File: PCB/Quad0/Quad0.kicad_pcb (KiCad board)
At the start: 4 copper layers, 50.1 x 50.1 mm, 97 parts, among them J1 DEBUG_CONN_PAD, J10 GPIO[23-24], J2 Mtype_Select, J3 Mtype_Select, J4 Mtype_Select, J5 Mtype_Select, J6 1N5819, J7 Power_Pad, J8 GPIO[18-22], J9 GPIO[27-29], Q1 DMN2024UFDF-7, Q2 DMN2024UFDF-7, Q3 DMN2024UFDF-7, Q4 DMN2024UFDF-7, SW1 RUN_BTN, SW2 BOOTSEL_BTN, U1 RP2350A_C42411118, U2 AP7361C-33E-13, U3 W25Q128JVSIQTR, U4 ABM8-272-T3_C20625731, U5 ICM-42688-P, U6 DPS368XTSA1, U7 BMM150, U8 ESP-01, U9 AP22818BKWT-7

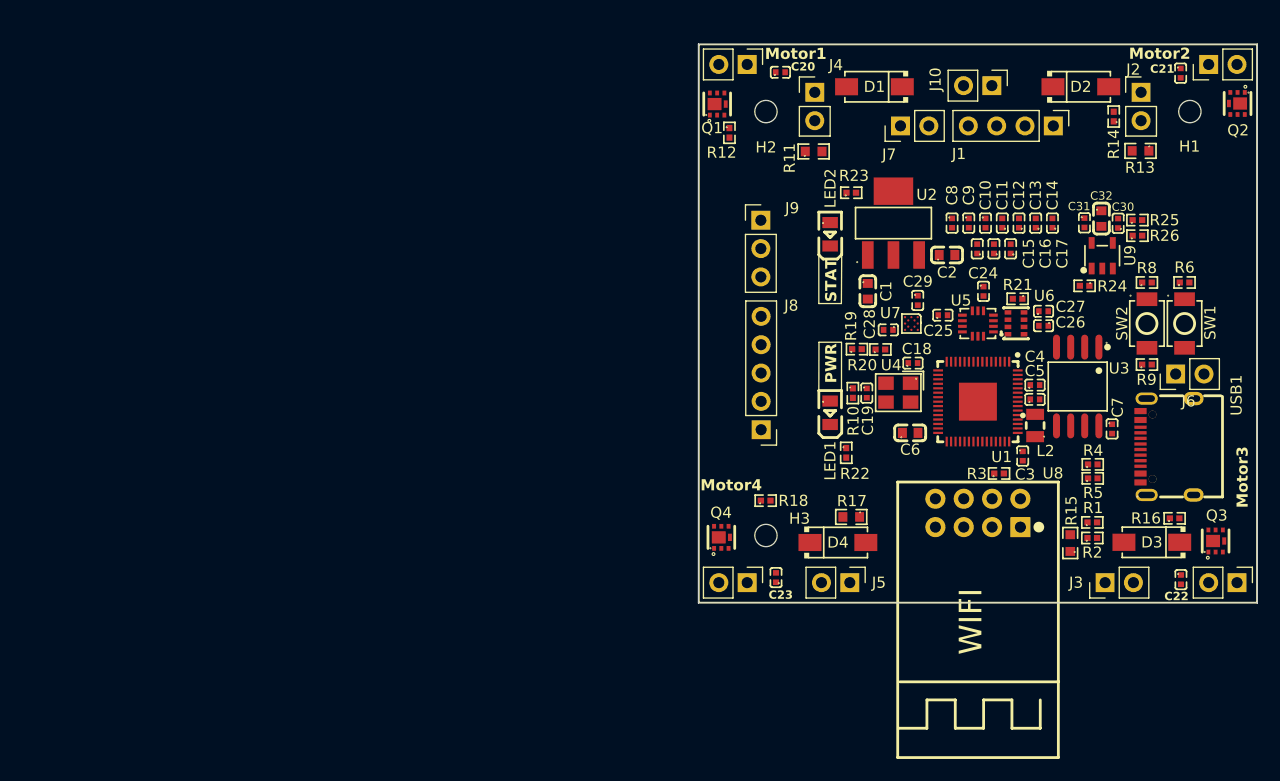
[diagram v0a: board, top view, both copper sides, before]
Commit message: pcb layout + routing v2
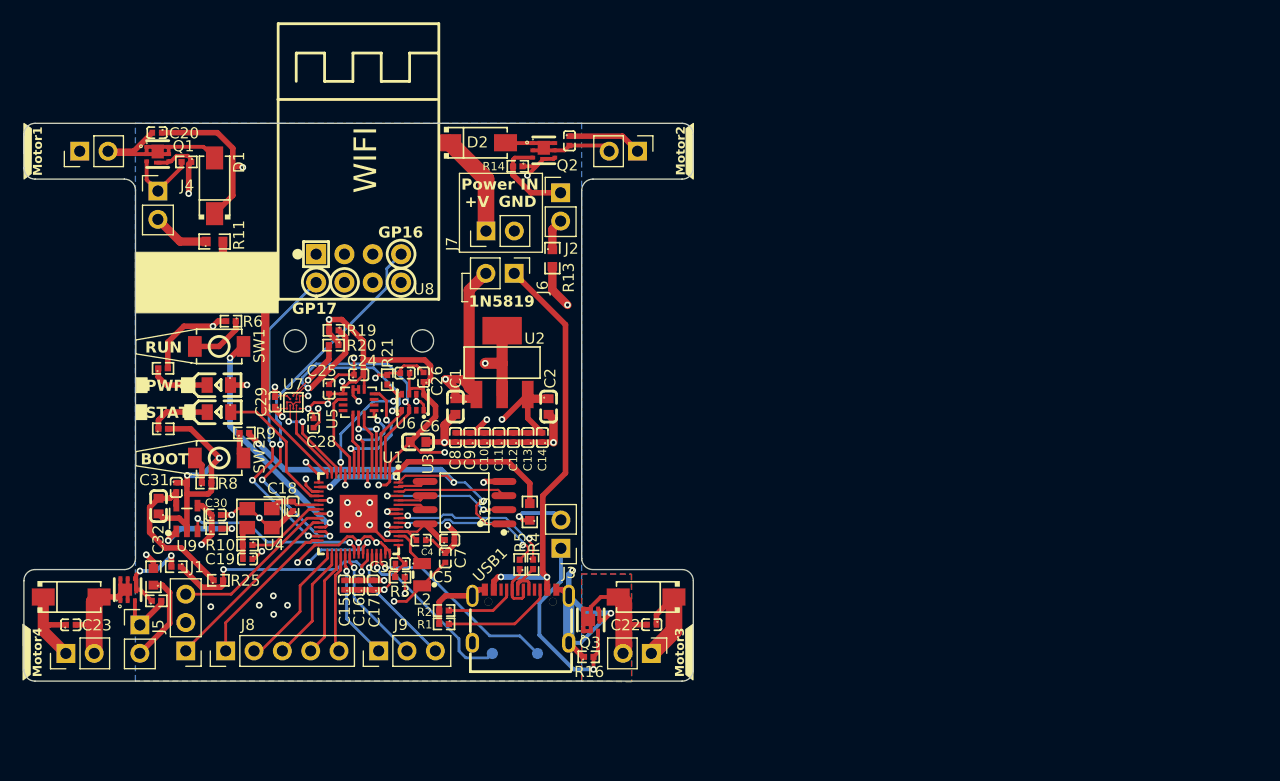
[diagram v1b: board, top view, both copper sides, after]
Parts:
- removed H3: MountingHole, MountingHole:MountingHole_2mm
- removed J10: GPIO[23-24], Connector_PinHeader_2.54mm:PinHeader_1x02_P2.54mm_Vertical
- added TP1: GPIO28_Pad, TestPoint:TestPoint_Pad_D1.0mm, B.Cu at (155.3, 120.8)
- added TP2: GPIO29_Pad, TestPoint:TestPoint_Pad_D1.0mm, B.Cu at (159.4, 120.8)
- J1: footprint Connector_PinHeader_2.54mm:PinHeader_1x04_P2.54mm_Vertical -> Connector_PinHeader_2.54mm:PinHeader_1x03_P2.54mm_Vertical
- J9: value GPIO[27-29] -> GPIO[23,24,27,28,29]
- moved R26 91.1 mm to (127.0, 113.0), turned to 180 degrees
- moved J1 90.9 mm to (127.9, 120.5), turned to 180 degrees
- moved R25 88.5 mm to (130.8, 114.2)
- moved C32 88.4 mm to (125.4, 107.5), turned to 90 degrees
- moved SW1 86.6 mm to (130.9, 93.2), turned to 180 degrees
- moved R8 86.2 mm to (129.7, 105.5)
- moved R6 85.6 mm to (131.9, 91.0), turned to 180 degrees
- moved U9 85.4 mm to (128.0, 108.7)
- moved C30 85.0 mm to (130.6, 108.3), turned to 0 degrees
- moved C31 84.8 mm to (127.0, 105.9)
- moved SW2 84.0 mm to (130.9, 103.2), turned to 180 degrees
- moved H1 82.8 mm to (137.7, 92.7)
- moved R9 81.1 mm to (133.1, 101.0)
- moved R24 80.8 mm to (130.6, 109.6), turned to 0 degrees
- moved D4 68.9 mm to (117.6, 115.7)
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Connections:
- net Net-(U1-USB_DM) renamed /USB_PICO-
- net Net-(U1-USB_DP) renamed /USB_PICO+
- J1 pad 1: GND -> /MCU_SWDIO
- J1 pad 3: /MCU_SWDIO -> /MCU_SWCLK
- J9 pad 1: /GPIO27 -> /GPIO23
- J9 pad 2: /GPIO28 -> /GPIO24
- J9 pad 3: /GPIO29 -> /GPIO27
- U1 pad 22: unconnected-(U1-XOUT-Pad22) -> /MCU_XOUT
- USB1 pad A4B9: +BATT_Brushed -> /USB_RAW_VBUS
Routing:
- net +BATT_Brushed: track 0.00 -> 207.9 mm, vias 0 -> 3
- net GND: track 0.00 -> 153.0 mm, vias 0 -> 35
- net +3.3V: track 0.00 -> 100.7 mm, vias 0 -> 18
- net +1V1: track 0.00 -> 45.8 mm, vias 0 -> 7
- net /USB_RAW_VBUS: track 0.00 -> 37.0 mm, vias 0 -> 2
- net /GPIO12: track 0.00 -> 35.6 mm, vias 0 -> 2
- net /GPIO16: track 0.00 -> 35.0 mm, vias 0 -> 3
- net /QSPI_SS: track 0.00 -> 33.5 mm, vias 0 -> 3
- net /BAR_SDA: track 0.00 -> 29.6 mm, vias 0 -> 2
- net /GPIO17: track 0.00 -> 28.4 mm, vias 0 -> 3
- net /GPIO11: track 0.00 -> 24.7 mm
- net /BAR_SCL: track 0.00 -> 24.6 mm, vias 0 -> 2
- net /GPIO13: track 0.00 -> 22.7 mm, vias 0 -> 2
- net /MCU_RUN: track 0.00 -> 21.4 mm, vias 0 -> 2
- net /BAT_SENSE_VD: track 0.00 -> 21.1 mm, vias 0 -> 2
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- added copper zone on In2.Cu, net +3.3V
- added copper zone on B.Cu, net GND
- added copper zone on F.Cu, net GND
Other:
- board size 50.1 x 50.1 mm -> 60 x 50 mm
- board text added: "+V"
- board text added: "1N5819"
- board text added: "BOOT"
- board text added: "GND"
- board text added: "GP16"
- board text added: "GP17"
- board text added: "Power IN"
- board text added: "RUN"

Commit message: pcb art + routing finished
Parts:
- added G***: LOGO, LOGO, F.Cu at (155.2, 102.4)
- added H3: MountingHole, MountingHole:MountingHole_2mm, F.Cu at (120.9, 80.2)
- added H4: MountingHole, MountingHole:MountingHole_2mm, F.Cu at (165.8, 80.2)
- moved C12 23.5 mm to (137.4, 114.0)
- moved C13 22.0 mm to (137.0, 106.0), turned to 0 degrees
- moved C14 19.0 mm to (140.9, 102.6), turned to -45 degrees
- moved C11 11.4 mm to (152.3, 112.2)
- moved C10 9.25 mm to (153.5, 110.6), turned to 180 degrees
- moved C9 3.01 mm to (150.3, 101.7), turned to -90 degrees
- moved C8 2.91 mm to (149.1, 101.8), turned to -90 degrees
- moved C6 1.19 mm to (147.5, 101.9), turned to 90 degrees
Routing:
- net +3.3V: track 100.7 -> 116.8 mm, vias 18 -> 17
- net GND: track 153.0 -> 164.3 mm, vias 35 -> 37
- added copper zone on In2.Cu, net +1V1
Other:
- outline, holes or cut-outs redrawn
- board text added: "18"
- board text added: "19"
- board text added: "20"
- board text added: "21"
- board text added: "22"
- board text added: "23"
- board text added: "24"
- board text added: "27"
- board text added: "28"
- board text added: "29"
- board text added: "Quad0"
- board text added: "SWCLK"
- board text added: "SWDIO"
- board text added: "[+]"
- board text added: "v1.0"
